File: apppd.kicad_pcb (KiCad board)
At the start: 4 copper layers, 58.9 x 48.4 mm, 103 parts, among them J1 Conn_SWD, J2 APPPD Connector, J4 2601-1102, J5 USB_C_Receptacle_USB2.0_16P, Q1 AO3400A, Q2 AO3400A, Q3 PMV100EPA, SW1 NRST, SW2 BOOT0, U1 AP2112K-3.3, U2 STM32F072CBTx, U3 USBLC6-2SC6, U4 TCAN337, U5 TLV9062xD, U6 LMR33610ADDAR, U7 TLV9062xD, Y1 ABM8AIG-24.000MHz-8-2Z-T

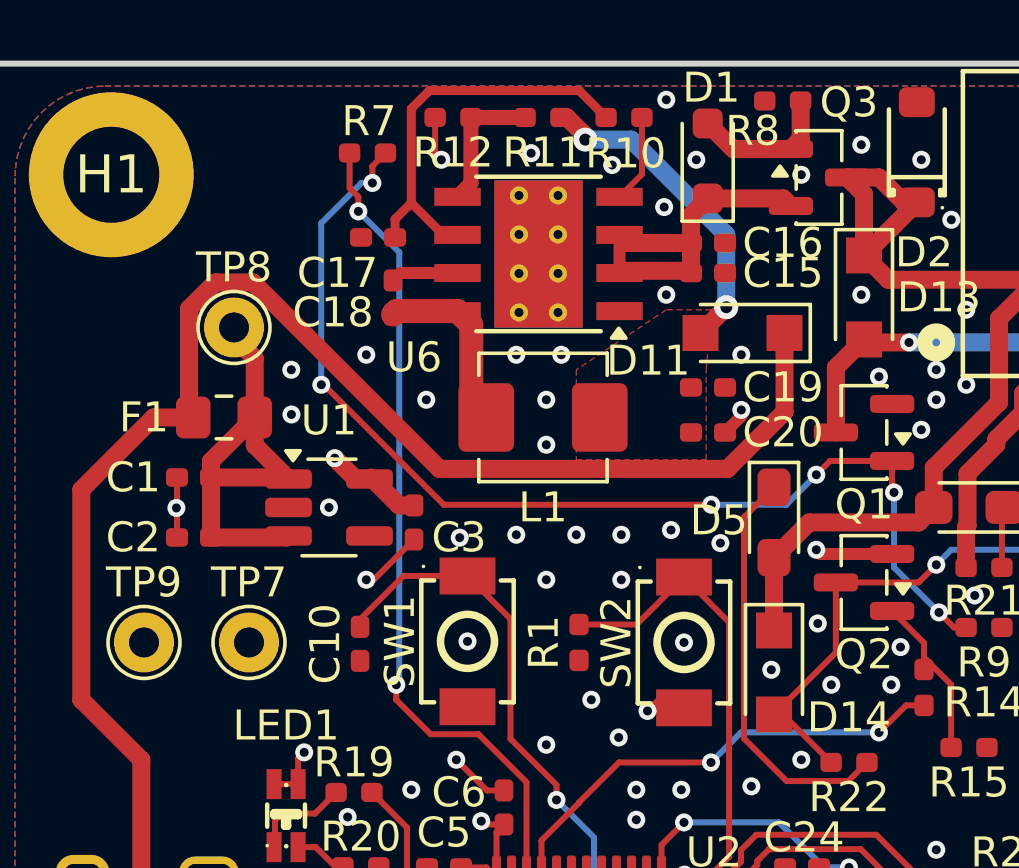
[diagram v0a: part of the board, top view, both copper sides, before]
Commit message: Swapped inductor due to availability
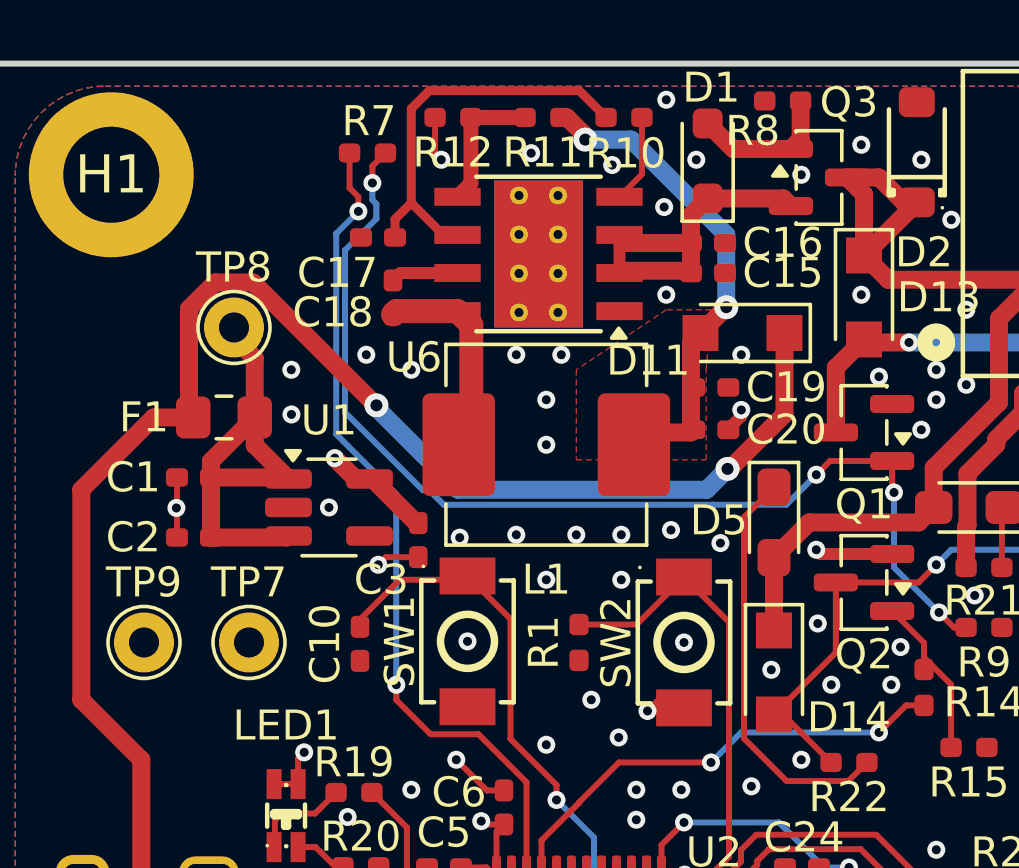
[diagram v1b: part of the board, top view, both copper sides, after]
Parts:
- L1: footprint Inductor_SMD:L_Vishay_IHLP-1616 -> Inductor_SMD:L_Vishay_IHLP-2525
- moved L1 0.92 mm to (30.5, 25.0)
- moved C3 0.61 mm to (26.2, 28.2)
- moved C20 0.14 mm to (36.0, 24.5)
- moved C19 0.11 mm to (36.0, 23.1)
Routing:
- net Net-(D11-A): track 10.8 -> 16.4 mm
- net GND: track 37.8 -> 37.0 mm
- net /SW: track 6.14 -> 5.43 mm
- net Net-(Q1-G): track 37.1 -> 36.4 mm, vias 6 -> 4
- net +5V: track 63.8 -> 64.5 mm, vias 0 -> 2
- net IGN_FET: track 27.6 -> 28.1 mm
